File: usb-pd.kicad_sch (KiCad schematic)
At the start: 39 parts, among them J3 USB-C_GCT_USB4105-GF-A, J4 JST_SH_1x4_SM04B-SRSS-TB-LF-SN, Q4 SQS401EN-T1_BE3, U2 TVS2200DRVR, U3 TVS2200DRVR, U4 TVS2200DRVR, U5 TPD4E02B04DQA, U6 STUSB4500_QFN

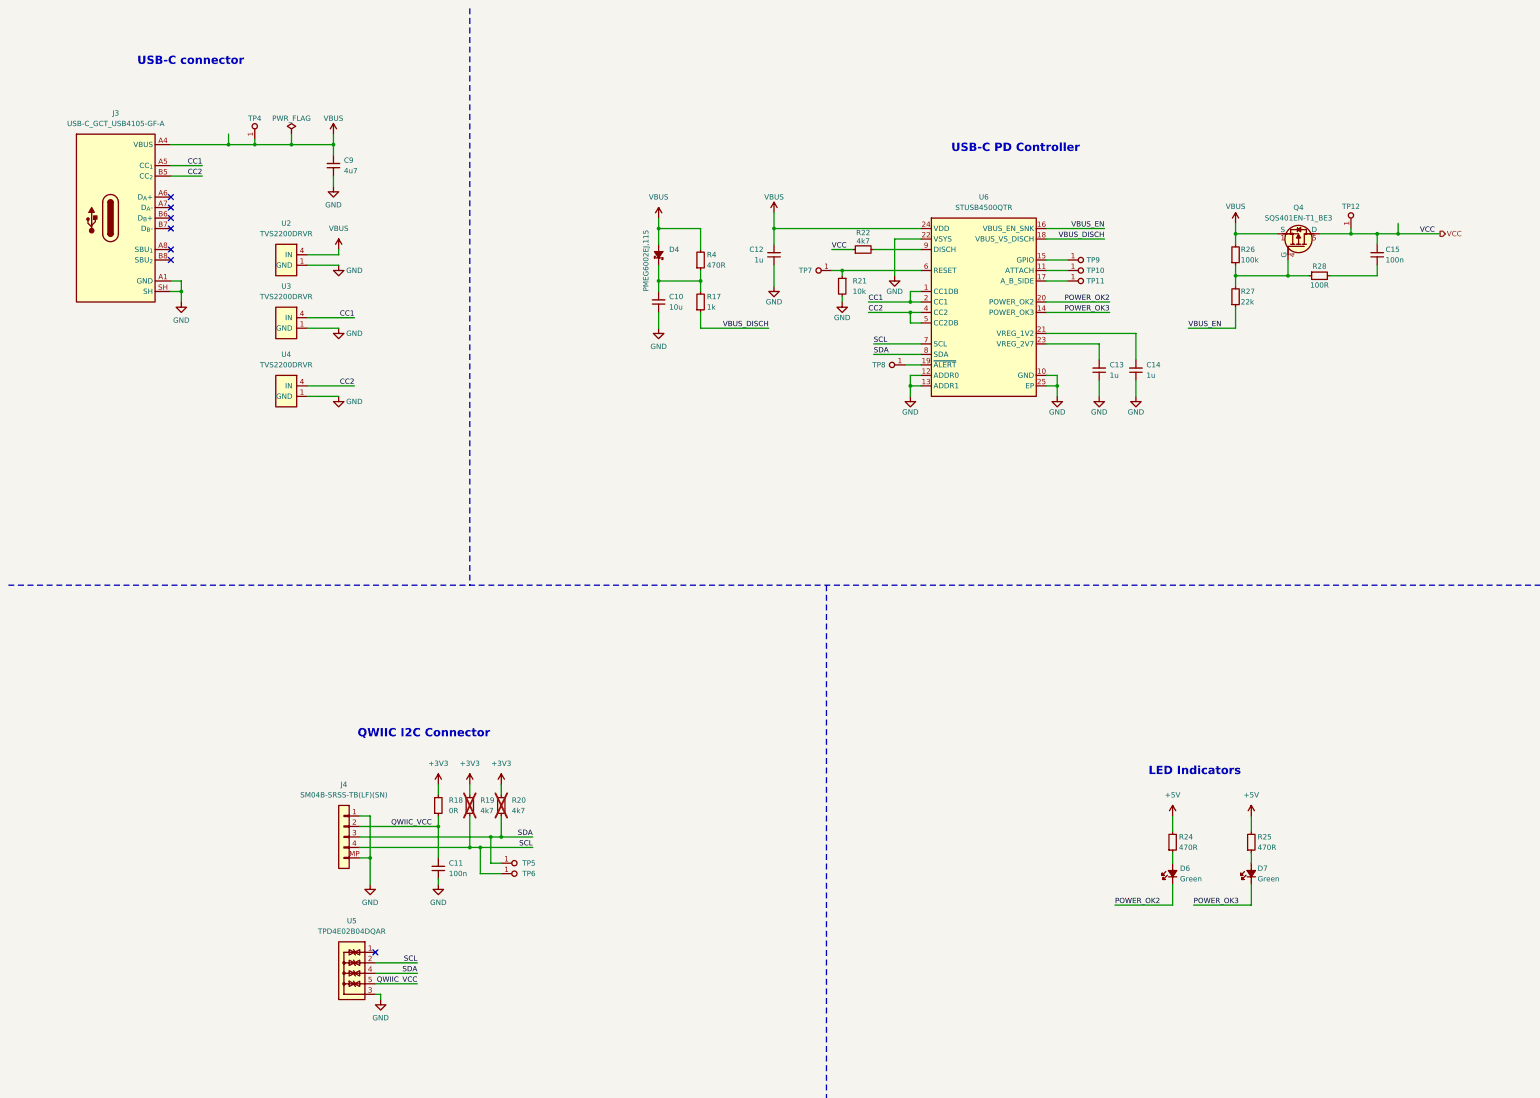
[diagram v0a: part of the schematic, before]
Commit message: [#79262] Change TVS diodes, adjust LEDs resistors, refactor USB-PD schematic
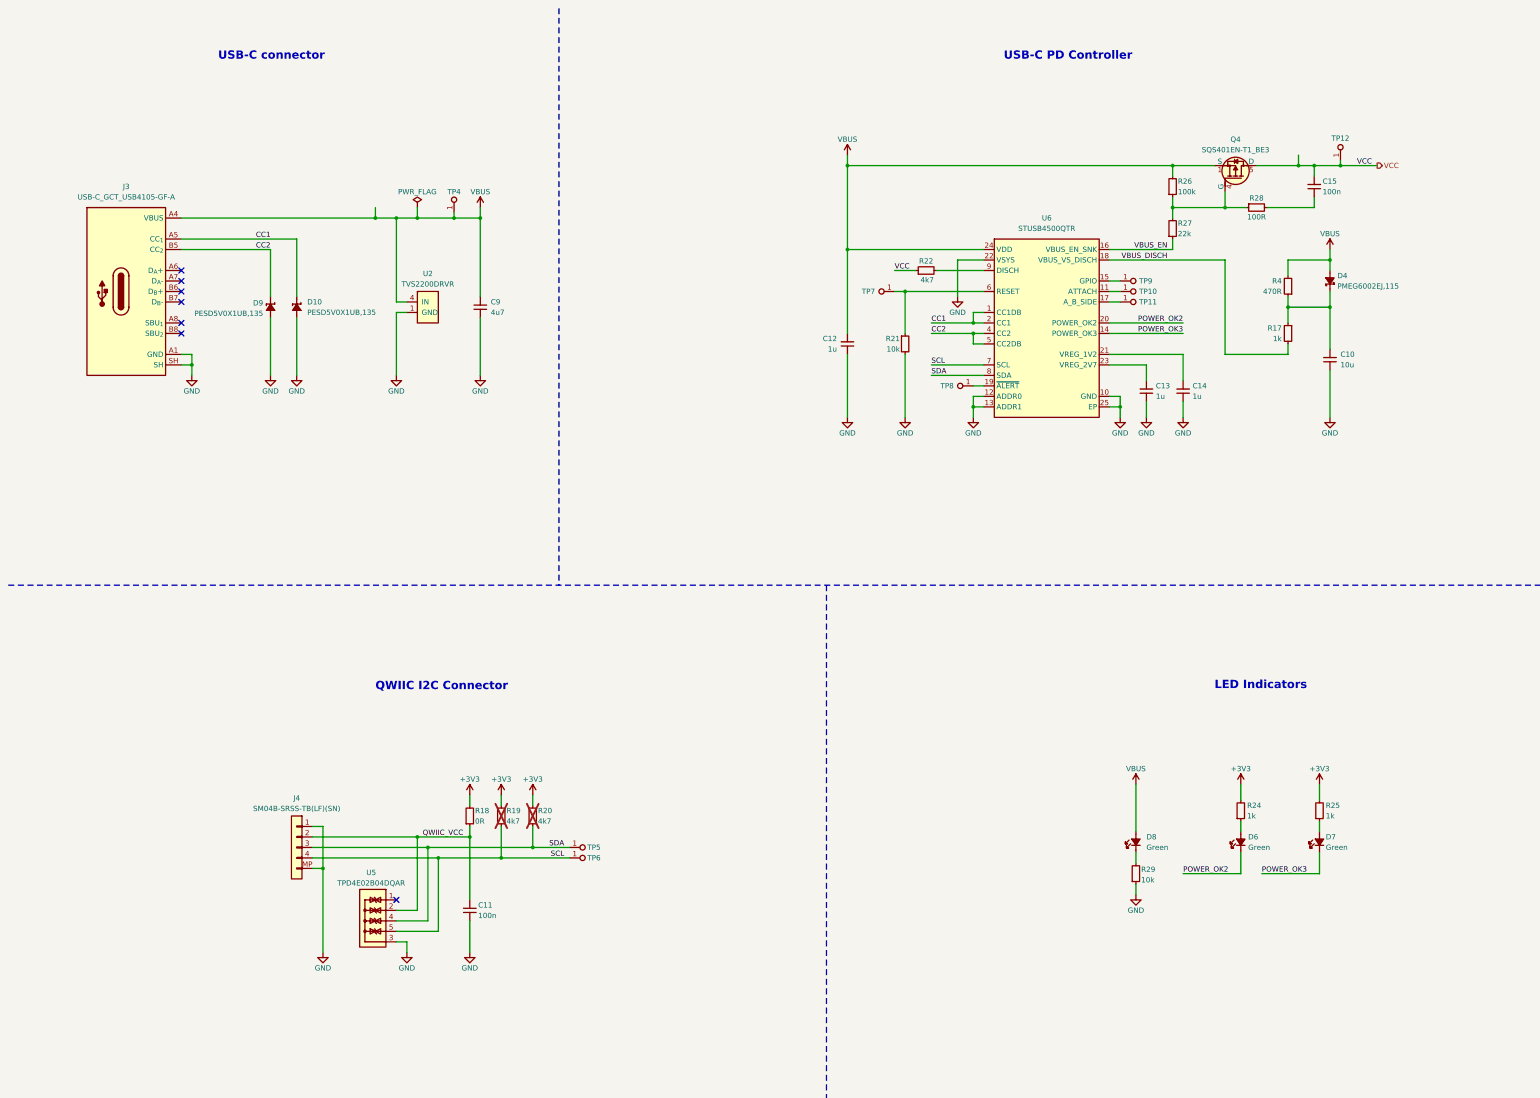
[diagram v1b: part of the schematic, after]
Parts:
- removed R24: R_470R_0402, antmicro-footprints:R_0402_1005Metric, symbol antmicroResistors0402:R_470R_0402
- removed R25: R_470_0402, antmicro-footprints:R_0402_1005Metric, symbol antmicroResistors0402:R_470R_0402
- removed U3, U4: TVS2200DRVR, antmicro-footprints:WSON-6-1EP_2x2mm_P0.65mm, symbol antmicroTVSDiodes:TVS2200DRVR
- added D10, D9: PESD5V0X1UB, antmicro-footprints:SOD-523, symbol antmicroTVSDiodes:PESD5V0X1UB
- added D8: LED_G_0603_LTST-C190GKT, antmicro-footprints:LED_0603_1608Metric_G, symbol antmicroLEDIndicationDiscrete:LED_G_0603_LTST-C190GKT
- added R24, R25: R_1k_0402, antmicro-footprints:R_0402_1005Metric, symbol antmicroResistors0402:R_1k_0402
- added R29: R_10k_0402, antmicro-footprints:R_0402_1005Metric, symbol antmicroResistors0402:R_10k_0402
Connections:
- net +3V3: now also R24.2, R25.2
- net CC1: now also D10.1 (C)
- net CC2: now also D9.1 (C)
- net GND: now also D10.2 (A), D9.2 (A), R29.1
- net QWIIC_VCC: now also U5.2, U5.9; no longer U5.5, U5.6
- net SCL: now also U5.5, U5.6; no longer U5.2, U5.9
- net VBUS: now also D8.2 (A)
- net VBUS_DISCH: now also R17.2; no longer R17.1
- net at C10.2, D4.1 (C), R4.1: now also R17.1; no longer R17.2
- net at D6.2 (A): now also R24.1
- net at D7.2 (A): now also R25.1
- new net: D8.1 (C), R29.2
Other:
- moved on the sheet: C10, C11, C12, C13, C14, C15, C9, D4, D6, D7, J3, J4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

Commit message: [#79262] Cleanup 12V DC-DC converter, move Molex connector to root sheet
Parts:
- added C16, C17, C18, C19, C28: C_22u_25V_0805, antmicro-footprints:C_0805_2012Metric, symbol antmicroCapacitorsmisc:C_22u_25V_0805
- added C20: C_1u_25V_0402, antmicro-footprints:C_0402_1005Metric, symbol antmicroCapacitors0402:C_1u_25V_0402
- added C21: C_4u7_25V_0402, antmicro-footprints:C_0402_1005Metric, symbol antmicroCapacitors0402:C_4u7_25V_0402
- added C22, C24, C25: C_10u_0805_35V, antmicro-footprints:C_0805_2012Metric, symbol antmicroCapacitorsmisc:C_10u_0805_35V
- added C23: C_33n_0402, antmicro-footprints:C_0402_1005Metric, symbol antmicroCapacitors0402:C_33n_0402
- added C26, C27, C31: C_100n_50V_X8L_0402, antmicro-footprints:C_0402_1005Metric, symbol antmicroCapacitors0402:C_100n_50V_X8L_0402
- added C29, C30, C43, C44: C_Pol_150u_30V_Vishay-T59-EE, antmicro-footprints:C_Pol_Vishay-T59-EE, symbol antmicroCapacitorspol:C_Pol_150u_30V_Vishay-T59-EE
- added L2: L_4u7_14.6A_Abracon-Q8080, antmicro-footprints:L_Abracon_ASPIAIG-Q8080, symbol antmicroFixedInductors:L_4u7_14.6A_Abracon-Q8080
- added R23: R_2k_0402, antmicro-footprints:R_0402_1005Metric, symbol antmicroResistors0402:R_2k_0402
- added R30: R_0R_0402, antmicro-footprints:R_0402_1005Metric, symbol antmicroResistors0402:R_0R_0402
- added R31: R_68k_0402, antmicro-footprints:R_0402_1005Metric, symbol antmicroResistors0402:R_68k_0402
- added R32, R34: R_100k_0402, antmicro-footprints:R_0402_1005Metric, symbol antmicroResistors0402:R_100k_0402
- added R33: R_158k_0402, antmicro-footprints:R_0402_1005Metric, symbol antmicroResistors0402:R_158k_0402
- added R36: R_3R3_0402, antmicro-footprints:R_0402_1005Metric, symbol antmicroResistors0402:R_3R3_0402
- added R39: R_10k_0.1%_0402, antmicro-footprints:R_0402_1005Metric, symbol antmicroResistors0402:R_10k_0.1%_0402
- added R40: R_140k_0.1%_0402, antmicro-footprints:R_0402_1005Metric, symbol antmicroResistors0402:R_140k_0.1%_0402
- added TP13: TP_0.75mm_SMD, antmicro-footprints:TP_SMD_0.75mm, symbol antmicroTestPoints:TP_0.75mm_SMD
- added U9: SIC477ED-T1-GE3, antmicro-footprints:SIC47XED-T1-GE3, symbol antmicroDCDCConverters:SIC477ED-T1-GE3
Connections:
- net GND: now also C16.1, C17.1, C18.1, C19.1, C20.1, C21.1, C22.1, C23.2, C24.1, C25.1, C26.1, C28.1, C29.2, C30.2, C31.1, C43.2, C44.2, R23.2, R31.1, R33.1, R39.1, U9.10 (PGND), U9.11 (PGND), U9.17 (PGND), U9.23 (AGND), U9.28 (AGND), U9.9 (PGND)
- net VCC: now also C22.2, C24.2, C25.2, C26.2, C43.1, C44.1, R32.2, U9.1 (V_{CIN}), U9.7 (V_{IN}), U9.8 (V_{IN})
- new net: C27.1, R36.1
- new net: R36.2, U9.5 (PHASE), U9.6 (PHASE)
- new net: C27.2, U9.4 (BOOT)
- new net 12V: C16.2, C17.2, C18.2, C19.2, C28.2, C29.1, C30.1, C31.2, L2.2, R40.2, TP13.1, U9.20 (V_{SNS})
- new net 12V_EN: R32.1, U9.3 (EN)
- new net 12V_FB: R39.2, R40.1, U9.22 (V_{FB})
- new net 12V_FSW: R33.2, U9.24 (f_{SW})
- new net 12V_ILIM: R30.2, R31.2, U9.25 (I_{LIMIT})
- new net 12V_MODE: R23.1, U9.27 (MODE)
- new net 12V_PG: R34.1, U9.2 (P_{GOOD})
- new net 12V_SS: C23.1, U9.19 (SS)
- new net 12V_SW: L2.1, U9.12 (SW), U9.13 (SW), U9.14 (SW)
- new net 12V_VDD: C20.2, R30.1, R34.2, U9.26 (V_{DD})
- new net 12V_VDRV: C21.2, U9.16 (V_{DRV})
- no-connect marks 7 -> 10
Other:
- note added: "+12V DC/DC converter"
- note added: "0.8V typ"
- note added: "Note: Place close to the feedback resistors"
- note added: "Output current: max 7A"
- note added: "Power save mode enabled, VDD, VDRVPre-reg on"
- note added: "R_FB_H = R_FB_L * (V_OUT - V_FB) / V_FB 10k * (12 - 0.8) / 0.8 = 140k"
- note added: "f_{sw} = 400kHz"
- moved on the sheet: C10, C11, C12, C13, C14, C15, D4, D6, D7, D8, J4, Q4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

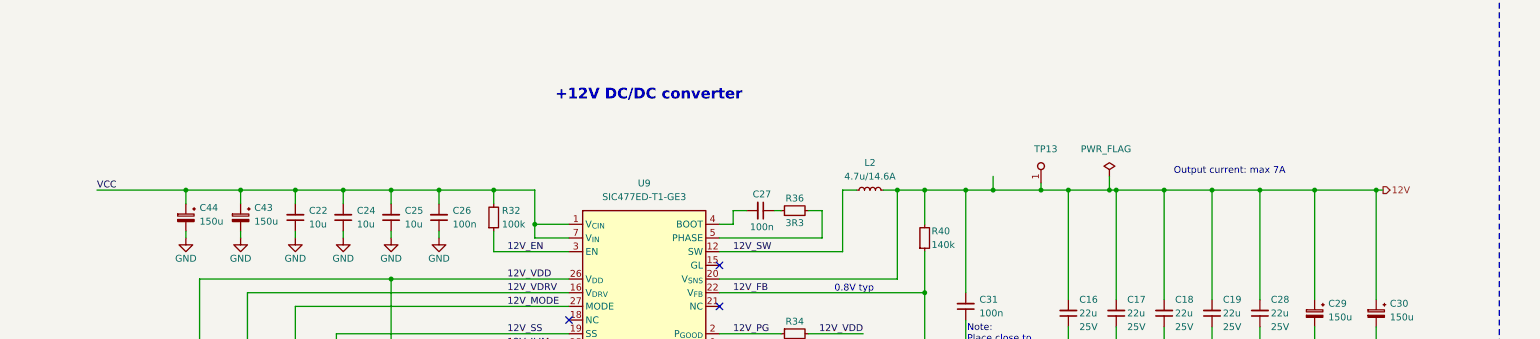
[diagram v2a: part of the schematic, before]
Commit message: [#79262] Finish power section schematic
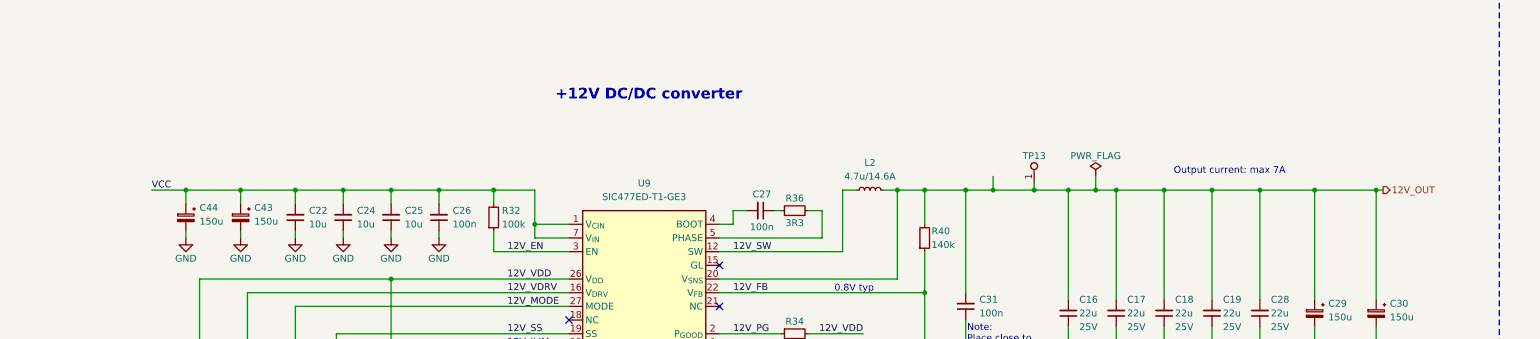
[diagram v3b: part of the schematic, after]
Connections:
- net 12V renamed 12V_OUT
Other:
- moved on the sheet: TP13
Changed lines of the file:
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@@
 	)
 	(junction
+		(at 203.2 194.31)
+		(diameter 0)
+		(color 0 0 0 0)
+	)
+	(junction
 		(at 66.04 194.31)
 		(diameter 0)
@@
 	)
 	(junction
+		(at 214.63 194.31)
+		(diameter 0)
+		(color 0 0 0 0)
+	)
+	(junction
 		(at 127 63.5)
 		(diameter 0)
@@
 	)
 	(junction
-		(at 217.17 194.31)
-		(diameter 0)
-		(color 0 0 0 0)
-	)
-	(junction
 		(at 83.82 194.31)
 		(diameter 0)
@@
 	)
 	(junction
-		(at 204.47 194.31)
-		(diameter 0)
-		(color 0 0 0 0)
-	)
-	(junction
 		(at 45.72 194.31)
 		(diameter 0)
@@
 	(wire
 		(pts
-			(xy 195.58 194.31) (xy 204.47 194.31)
+			(xy 195.58 194.31) (xy 203.2 194.31)
 		)
 		(stroke
@@
 	(wire
 		(pts
+			(xy 203.2 194.31) (xy 209.55 194.31)
+		)
+		(stroke
+			(width 0)
+			(type default)
+		)
+	)
+	(wire
+		(pts
 			(xy 386.08 73.66) (xy 386.08 76.2)
 		)
@@
 	(wire
 		(pts
+			(xy 214.63 194.31) (xy 218.44 194.31)
+		)
+		(stroke
+			(width 0)
+			(type default)
+		)
+	)
+	(wire
+		(pts
 			(xy 48.26 210.82) (xy 83.82 210.82)
 		)
@@
 		)
 	)
-	(wire
-		(pts
-			(xy 204.47 194.31) (xy 209.55 194.31)
-		)
-		(stroke
-			(width 0)
-			(type default)
-		)
-	)
 	(polyline
 		(pts
@@
 	(wire
 		(pts
-			(xy 29.21 194.31) (xy 45.72 194.31)
+			(xy 39.37 194.31) (xy 45.72 194.31)
 		)
 		(stroke
@@
 	(wire
 		(pts
-			(xy 217.17 191.77) (xy 217.17 194.31)
+			(xy 214.63 191.77) (xy 214.63 194.31)
 		)
 		(stroke
@@
 	(wire
 		(pts
-			(xy 204.47 193.04) (xy 204.47 194.31)
+			(xy 203.2 193.04) (xy 203.2 194.31)
 		)
 		(stroke
@@
 	(wire
 		(pts
-			(xy 209.55 194.31) (xy 217.17 194.31)
+			(xy 209.55 194.31) (xy 214.63 194.31)
 		)
 		(stroke
@@
 	(wire
 		(pts
-			(xy 217.17 194.31) (xy 218.44 194.31)
-		)
-		(stroke
-			(width 0)
-			(type default)
-		)
-	)
-	(wire
-		(pts
 			(xy 83.82 210.82) (xy 116.84 210.82)
 		)
@@
 	)
 	(label "VCC"
-		(at 29.21 194.31 0)
+		(at 39.37 194.31 0)
 		(effects
 			(font
@@
 		)
 	)
-	(hierarchical_label "12V"
+	(hierarchical_label "12V_OUT"
 		(shape output)
 		(at 267.97 194.31 0)
@@
 	(symbol
 		(lib_id "antmicropower:PWR_FLAG")
-		(at 217.17 191.77 0)
+		(at 214.63 191.77 0)
 		(unit 1)
 		(exclude_from_sim no)
@@
 		(dnp no)
 		(property "Reference" "#FLG07"
-			(at 217.17 189.865 0)
+			(at 214.63 189.865 0)
 			(effects
 				(font
@@
 		)
 		(property "Value" "PWR_FLAG"
-			(at 216.535 186.69 0)
+			(at 214.63 187.96 0)
 			(effects
 				(font
@@
 		)
 		(property "Footprint" ""
-			(at 217.17 191.77 0)
+			(at 214.63 191.77 0)
 			(effects
 				(font
@@
 		)
 		(property "Datasheet" ""
-			(at 217.17 191.77 0)
+			(at 214.63 191.77 0)
 			(effects
 				(font
@@
 		)
 		(property "Description" ""
-			(at 217.17 191.77 0)
+			(at 214.63 191.77 0)
 			(effects
 				(font
@@
 	(symbol
 		(lib_id "antmicroTestPoints:TP_0.75mm_SMD")
-		(at 204.47 193.04 90)
+		(at 203.2 193.04 90)
 		(unit 1)
 		(exclude_from_sim no)
@@
 		(dnp no)
 		(property "Reference" "TP13"
-			(at 203.2 186.69 90)
+			(at 203.2 187.96 90)
 			(effects
 				(font
@@
 					(thickness 0.15)
 				)
-				(justify right)
 			)
 		)
 		(property "Value" "TP_0.75mm_SMD"
-			(at 208.28 182.245 0)
+			(at 207.01 182.245 0)
 			(effects
 				(font
@@
 		)
 		(property "Footprint" "antmicro-footprints:TP_SMD_0.75mm"
-			(at 210.82 182.245 0)
+			(at 209.55 182.245 0)
 			(effects
 				(font
@@
 		)
 		(property "Datasheet" ""
-			(at 217.17 175.26 0)
+			(at 215.9 175.26 0)
 			(effects
 				(font
@@
 		)
 		(property "Description" "SMT test point"
-			(at 204.47 193.04 0)
+			(at 203.2 193.04 0)
 			(effects
 				(font
@@
 		)
 		(property "MPN" ""
-			(at 215.9 182.245 0)
+			(at 214.63 182.245 0)
 			(effects
 				(font
@@
 		)
 		(property "Manufacturer" ""
-			(at 210.82 182.245 0)
+			(at 209.55 182.245 0)
 			(effects
 				(font
@@
 		)
 		(property "Author" "Antmicro"
-			(at 213.36 182.245 0)
+			(at 212.09 182.245 0)
 			(effects
 				(font
@@
 		)
 		(property "License" "Apache-2.0"
-			(at 215.9 182.245 0)
+			(at 214.63 182.245 0)
 			(effects
 				(font
@@
 	)
 	(symbol
-		(lib_name "R_10k_0402_3")
 		(lib_id "antmicroResistors0402:R_10k_0402")
 		(at 323.85 224.79 90)
